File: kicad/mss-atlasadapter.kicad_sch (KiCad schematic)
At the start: 37 parts, among them J1 Screw_Terminal_01x02, U1 AP7381-50Y, U3 74HC4049, U4 AP3012

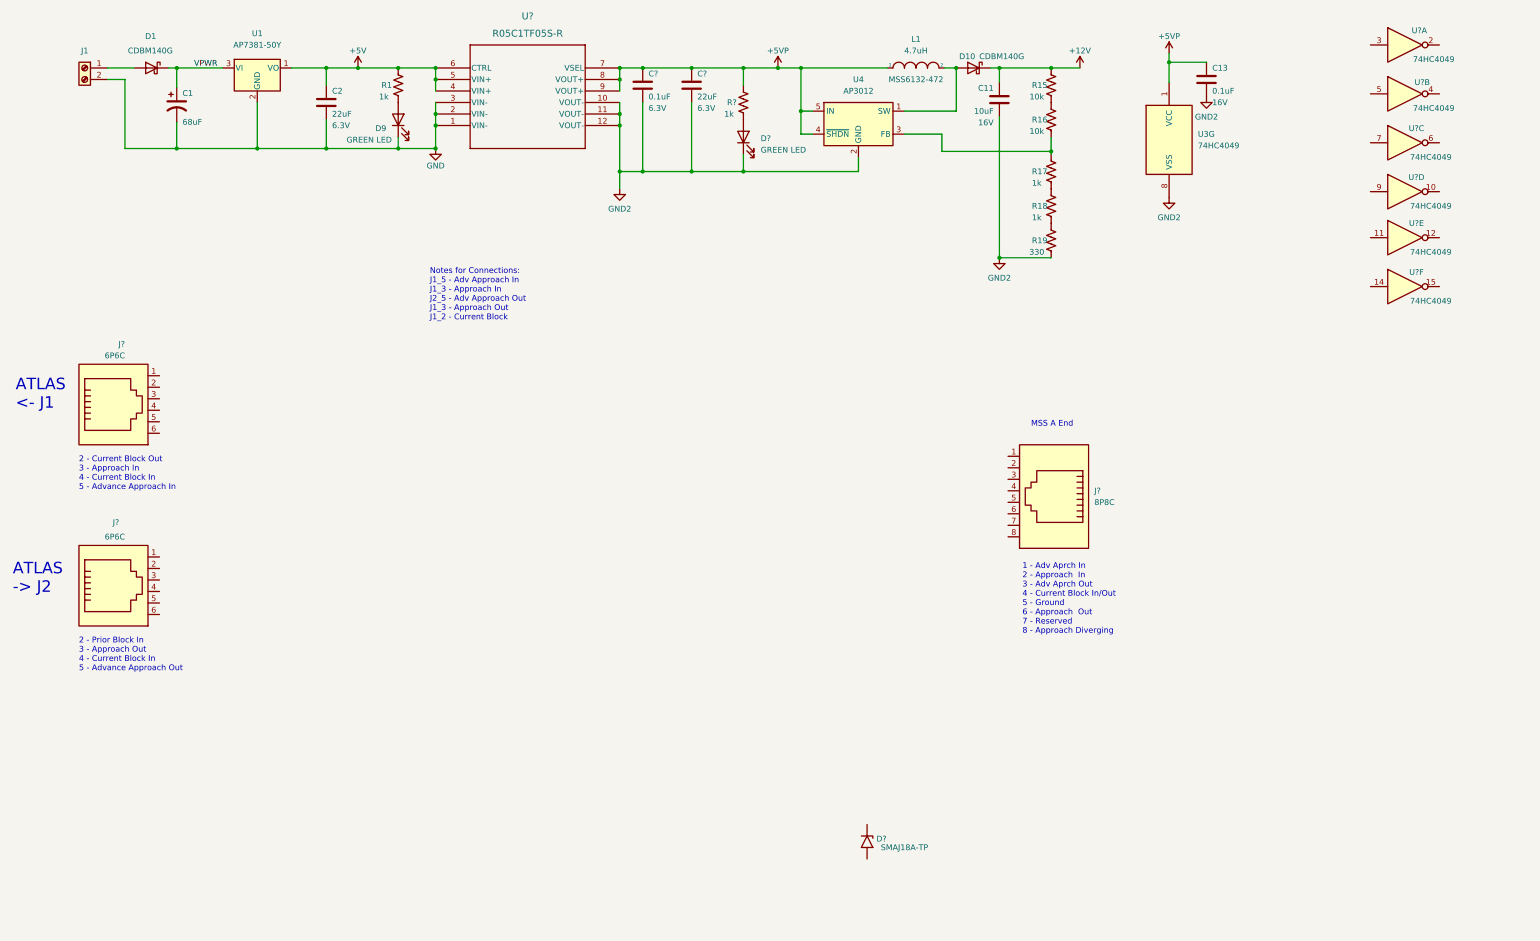
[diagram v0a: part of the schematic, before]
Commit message: Initial cut of what I think is a working circuit
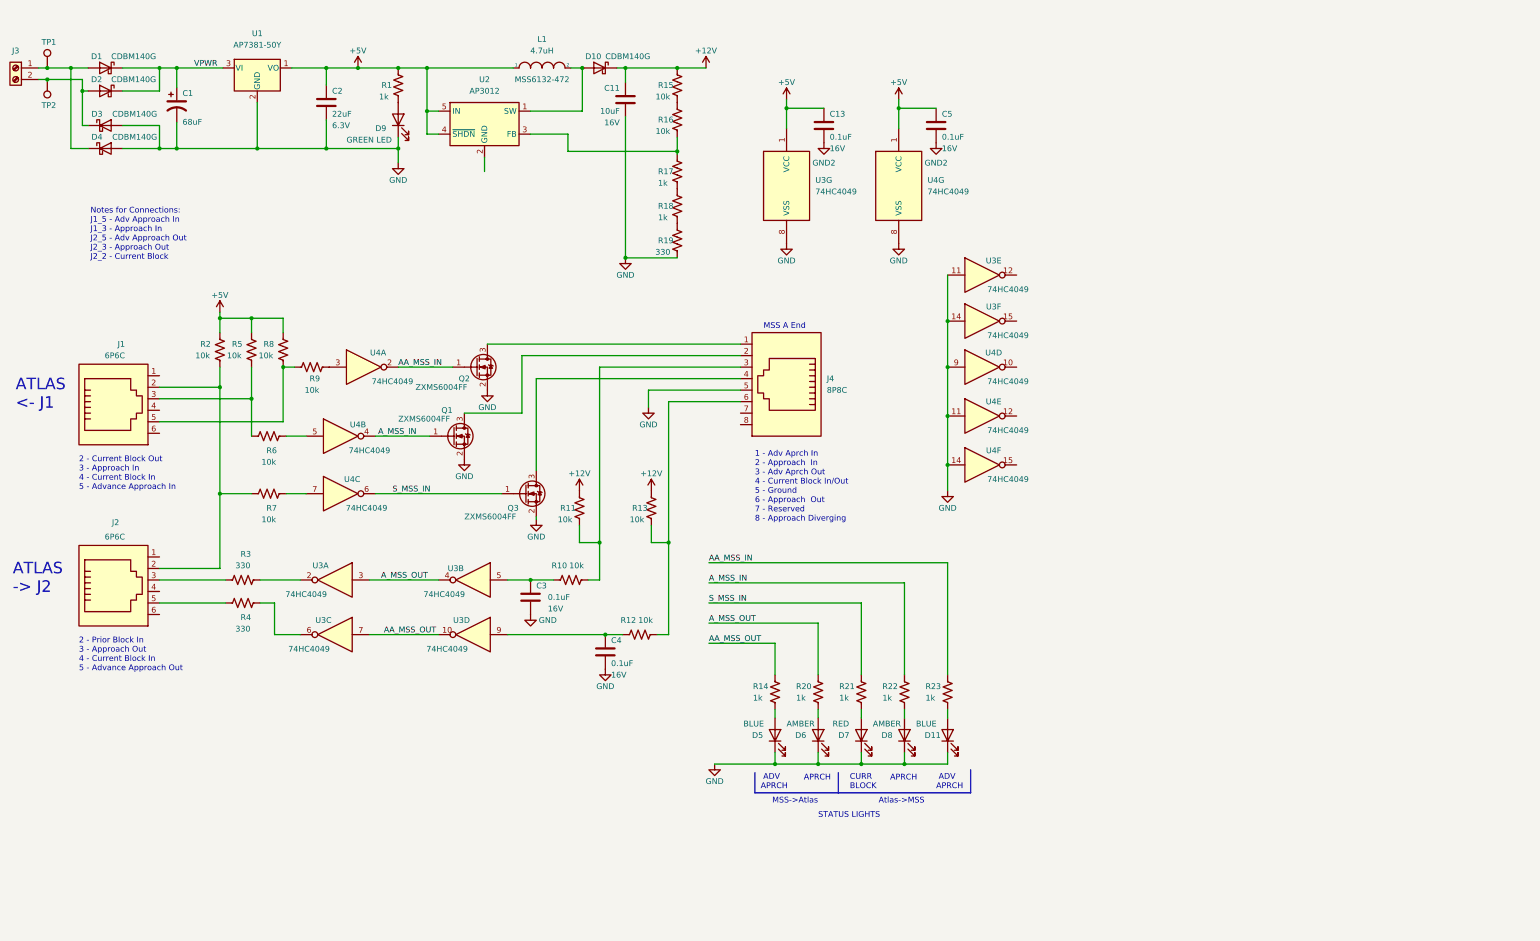
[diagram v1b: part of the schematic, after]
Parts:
- removed C?: 22uF, Capacitor_SMD:C_0805_2012Metric, symbol Device:C
- removed C?: 0.1uF, Capacitor_SMD:C_0805_2012Metric, symbol Device:C
- removed D?: GREEN LED, LED_SMD:LED_0805_2012Metric, symbol Device:LED
- removed D?: SMAJ18A-TP, Diode_SMD:D_SMA, symbol Diode:SM6T75A
- removed J1: Screw_Terminal_01x02, TerminalBlock_RND:TerminalBlock_RND_205-00012_1x02_P5.00mm_Horizontal, symbol Connector:Screw_Terminal_01x02
- removed R?: 1k, Resistor_SMD:R_0805_2012Metric, symbol Device:R_US
- removed U?: R05C1TF05S-R, ISE_UltraLibrarian:11-5B201S_TOS, symbol ISE_UltraLibrarian:R05C1TF05S-R
- removed U? (x5): 74HC4049, symbol 4xxx:4049
- removed U?: 74HC4049, Package_SO:SO-16_3.9x9.9mm_P1.27mm, symbol 4xxx:4049
- added C3, C4, C5: 0.1uF, Capacitor_SMD:C_0805_2012Metric, symbol Device:C
- added D11, D5: BLUE, LED_SMD:LED_0805_2012Metric, symbol Device:LED
- added D2, D3, D4: CDBM140G, Diode_SMD:D_SOD-123, symbol Device:D_Schottky
- added D6, D8: AMBER, LED_SMD:LED_0805_2012Metric, symbol Device:LED
- added D7: RED, LED_SMD:LED_0805_2012Metric, symbol Device:LED
- added J3: Screw_Terminal_01x02, TerminalBlock_RND:TerminalBlock_RND_205-00012_1x02_P5.00mm_Horizontal, symbol Connector:Screw_Terminal_01x02
- added Q1, Q2, Q3: ZXMS6004FF, Package_TO_SOT_SMD:SOT-23, symbol Transistor_FET:ZXM61N02F
- added R10, R11, R12, R13, R2, R5, R6, R7, R8, R9: 10k, Resistor_SMD:R_0805_2012Metric, symbol Device:R_US
- added R14, R20, R21, R22, R23: 1k, Resistor_SMD:R_0805_2012Metric, symbol Device:R_US
- added R3, R4: 330, Resistor_SMD:R_0805_2012Metric, symbol Device:R_US
- added TP1, TP2: TestPoint, TestPoint:TestPoint_Pad_D2.0mm, symbol Connector:TestPoint
- added unit 6 of U3
- added unit 5 of U3
- added unit 2 of U3
- added unit 1 of U3
- added unit 4 of U3
- added unit 3 of U3
- added U4: 74HC4049, symbol 4xxx:4049
- gave numbers to parts that had none: 3
- renumbered U4 to U2
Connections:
- net +5VP is gone; now on net +5V: C13.1, L1.1, U2.4 (~{SHDN}), U2.5 (IN), U3.1 (VCC)
- net +12V: now also R11.2, R13.2
- net +5V: now also C5.1, R2.1, R5.1, R8.1, U4.1 (VCC)
- net GND: now also C11.2, J4.5, R19.1, U3.8 (VSS), C3.2, C4.2, D11.1 (K), D3.2 (A), D4.2 (A), D5.1 (K), D6.1 (K), D7.1 (K), D8.1 (K), Q1.2 (S), Q2.2 (S), Q3.2 (S), U3.11, U3.14, U4.11, U4.14, U4.8 (VSS), U4.9
- net GND2: now also C5.2; no longer C11.2, R19.1, U2.2 (GND), U3.8 (VSS)
- net VPWR: now also D2.1 (K)
- net at J2.2: now also J1.2, R2.2, R7.2
- net at J2.3: now also R3.2
- net at J2.5: now also R4.2
- net at J1.3: now also R5.2, R6.2
- net at J1.5: now also R8.2, R9.1
- net at D1.2 (A): now also D4.1 (K), J3.1 (Pin_1), TP1.1
- net at J4.1: now also Q2.3 (D)
- net at J4.2: now also Q1.3 (D)
- net at J4.3: now also R10.1, R11.1
- net at J4.4: now also Q3.3 (D)
- net at J4.6: now also R12.1, R13.1
- new net: D11.2 (A), R23.2
- new net: D2.2 (A), D3.1 (K), J3.2 (Pin_2), TP2.1
- new net: D8.2 (A), R22.2
- new net: C4.1, R12.2, U3.9
- new net: C3.1, R10.2, U3.5
- new net: D6.2 (A), R20.2
- new net: R9.2, U4.3
- new net: D5.2 (A), R14.2
- new net: R3.1, U3.2
- new net: R7.1, U4.7
- new net: R6.1, U4.5
- new net: R4.1, U3.6
- new net: D7.2 (A), R21.2
- new net AA_MSS_IN: Q2.1 (G), R23.1, U4.2
- new net AA_MSS_OUT: R14.1, U3.10, U3.7
- new net A_MSS_IN: Q1.1 (G), R22.1, U4.4
- new net A_MSS_OUT: R20.1, U3.3, U3.4
- new net S_MSS_IN: Q3.1 (G), R21.1, U4.6
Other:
- note added: "ADV APRCH"
- note added: "APRCH"
- note added: "Atlas->MSS"
- note added: "CURR BLOCK"
- note added: "MSS->Atlas"
- note added: "Notes for Connections: J1_5 - Adv Approach In J1_3 - Approach In J2_5 - Adv Approach Out J2_3 - Approach Out J2_2 - Current Block"
- note added: "STATUS LIGHTS"
- note removed: "Notes for Connections: J1_5 - Adv Approach In J1_3 - Approach In J2_5 - Adv Approach Out J1_3 - Approach Out J1_2 - Current Block"
- title: MSS Cascade Basic v1.0 -> MSS Atlas Signal Adapter v1.0
- moved on the sheet: C11, C13, D10, J4, L1, R15, R16, R17, R18, R19, U2, U3G

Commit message: First cut at board layout for the adapter
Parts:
- added C6, C7, C8: 0.1uF, Capacitor_SMD:C_0805_2012Metric, symbol Device:C
- D1, D10, D2, D3, D4: footprint Diode_SMD:D_SOD-123 -> ISE_Generic:SOD-123T
- J1, J2: footprint (none) -> Connector_RJ:RJ12_Amphenol_54601
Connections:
- net GND2 is gone; now on net GND: C13.2, C5.2
- net AA_MSS_IN: now also U4.6; no longer U4.2
- net AA_MSS_OUT: now also U3.15; no longer U3.10
- net GND: now also U2.2 (GND), U3.9, C6.2, C7.2, C8.2; no longer U3.14
- net S_MSS_IN: now also U4.2; no longer U4.6
- net at C4.1, R12.2: now also U3.14; no longer U3.9
- net at U4.3: now also R7.1, C6.1; no longer R9.2
- net at U4.7: now also R9.2, C8.1; no longer R7.1
- net at R6.1, U4.5: now also C7.1
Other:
- note added: "2 - Current Block Out 3 - Approach In 4 - Force Red In 5 - Advance Approach In"
- note added: "2 - Prior Block In 3 - Approach Out 4 - Force Red In 5 - Advance Approach Out"
- note removed: "2 - Current Block Out 3 - Approach In 4 - Current Block In 5 - Advance Approach In"
- note removed: "2 - Prior Block In 3 - Approach Out 4 - Current Block In 5 - Advance Approach Out"
- moved on the sheet: C3, C4, J4, Q1, Q2, Q3, R10, R11, R12, R13, R9, U3A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

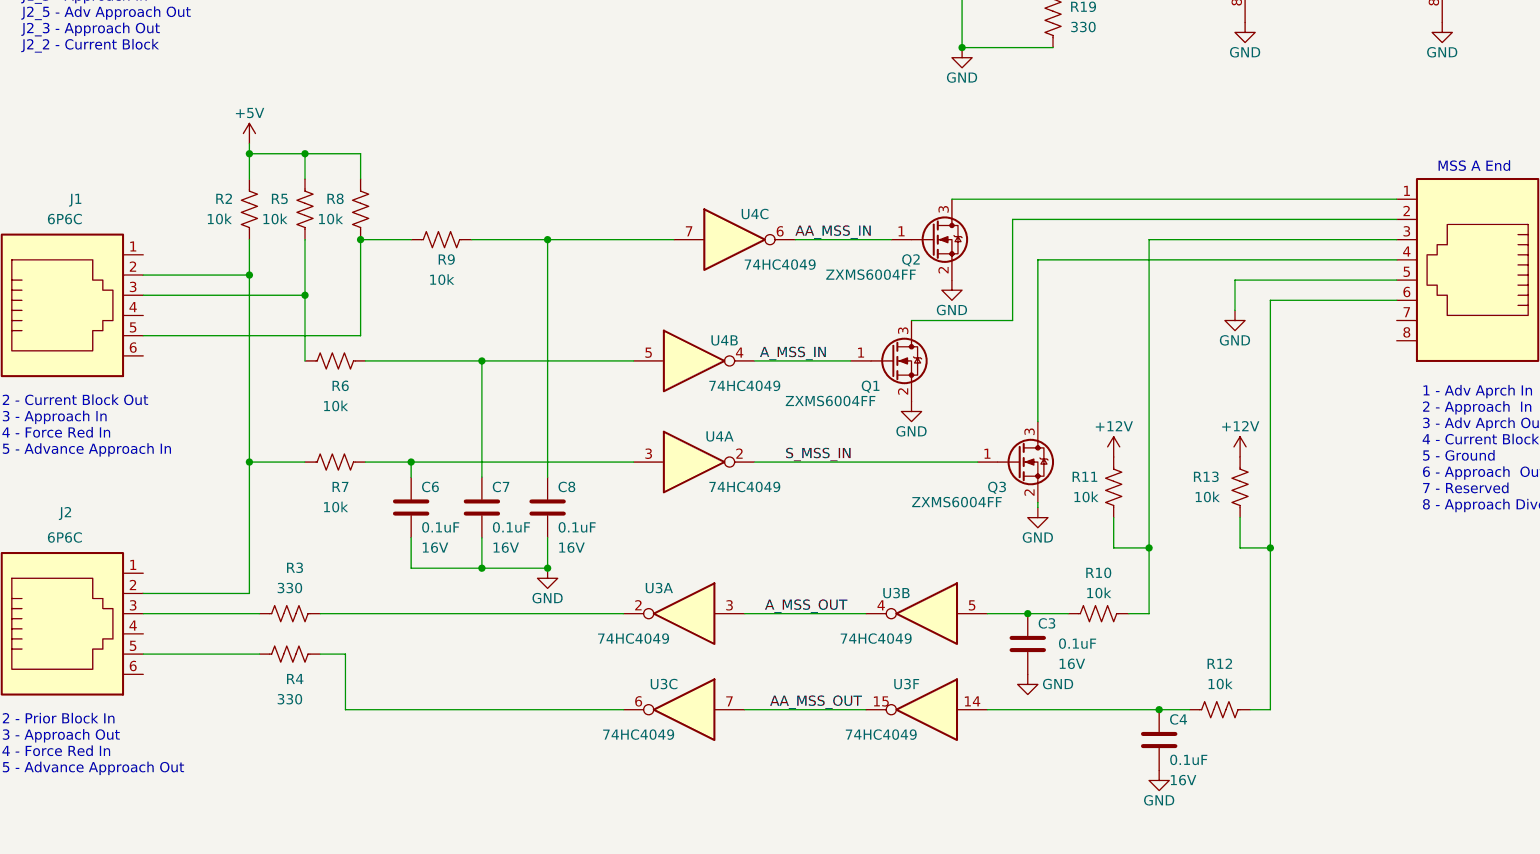
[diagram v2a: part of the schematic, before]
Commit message: Add test points
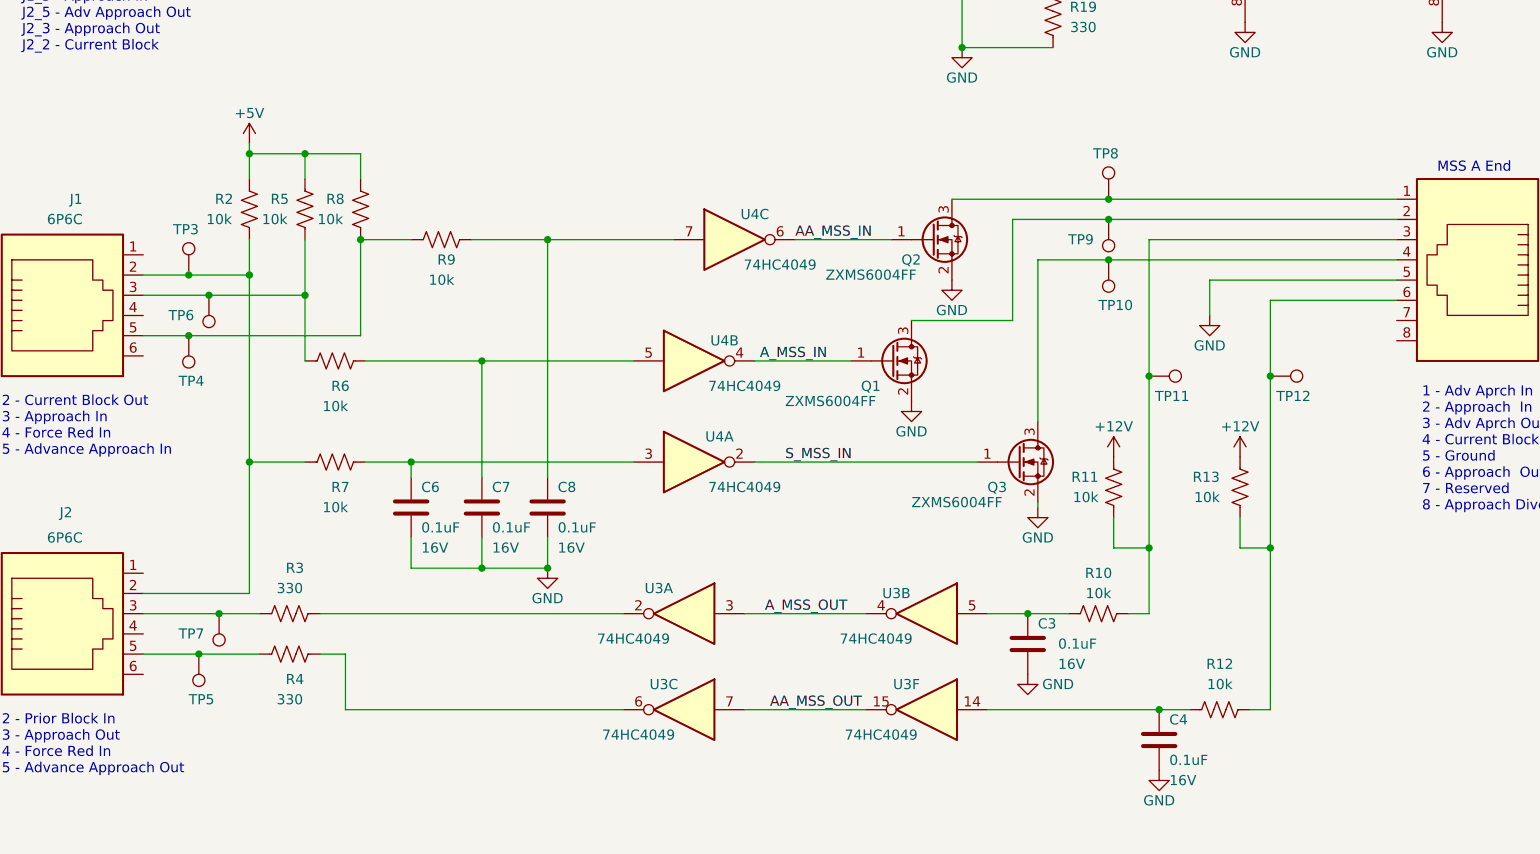
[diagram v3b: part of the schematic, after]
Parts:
- added TP10, TP11, TP12, TP3, TP4, TP5, TP6, TP7, TP8, TP9: TestPoint, TestPoint:TestPoint_Pad_D2.0mm, symbol Connector:TestPoint
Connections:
- net at J1.2, J2.2, R2.2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: now also TP3.1
- net at J2.3, R3.2: now also TP7.1
- net at J2.5, R4.2: now also TP5.1
- net at J1.3, R5.2, R6.2: now also TP6.1
- net at J1.5, R8.2, R9.1: now also TP4.1
- net at J4.3, R10.1, R11.1: now also TP11.1
- net at J4.2, Q1.3 (D): now also TP9.1
- net at J4.6, R12.1, R13.1: now also TP12.1
- net at J4.4, Q3.3 (D): now also TP10.1
- net at J4.1, Q2.3 (D): now also TP8.1
